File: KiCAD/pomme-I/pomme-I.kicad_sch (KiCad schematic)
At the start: 32 parts, among them J1 TV out, Q1 2N3904, SW1 SW_SPST, SW2 reset, SW3 local echo, SW4 baud rate 1, SW5 baud rate 0, T1 step down transformer, U1 LD1117V50-TO-220, U2 23LC1024, U3 25LC1024, Y1 20 Mhz

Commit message: modification schémitique
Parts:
- added D5, D6: 1N4001, Diode_THT:D_DO-41_SOD81_P10.16mm_Horizontal, symbol Diode:1N4004
- D1, D2: value 1N4004 -> 1N4001
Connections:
- net Vunreg: now reaches C1.1, D1.1 (K), D2.1 (K), U1.3 (VI)
- net Vunreg: now also D5.2 (A), D6.2 (A)
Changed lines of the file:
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@@
     (stroke (width 0) (type default) (color 0 0 0 0))
   )
+  (wire (pts (xy 106.68 124.46) (xy 106.68 114.3))
+    (stroke (width 0) (type default) (color 0 0 0 0))
+  )
   (polyline (pts (xy 153.035 39.37) (xy 169.545 39.37))
     (stroke (width 0) (type solid) (color 0 0 0 0))
@@
     (stroke (width 0) (type default) (color 0 0 0 0))
   )
+  (wire (pts (xy 156.845 60.96) (xy 156.845 53.34))
+    (stroke (width 0) (type default) (color 0 0 0 0))
+  )
   (wire (pts (xy 114.935 142.875) (xy 114.935 149.86))
     (stroke (width 0) (type default) (color 0 0 0 0))
@@
     (stroke (width 0) (type default) (color 0 0 0 0))
   )
+  (wire (pts (xy 106.68 114.3) (xy 102.87 114.3))
+    (stroke (width 0) (type default) (color 0 0 0 0))
+  )
   (wire (pts (xy 161.29 154.305) (xy 161.29 156.845))
     (stroke (width 0) (type default) (color 0 0 0 0))
@@
     (stroke (width 0) (type default) (color 0 0 0 0))
   )
+  (wire (pts (xy 154.305 53.34) (xy 156.845 53.34))
+    (stroke (width 0) (type default) (color 0 0 0 0))
+  )
   (wire (pts (xy 197.485 46.99) (xy 188.595 46.99))
     (stroke (width 0) (type default) (color 0 0 0 0))
@@
     (effects (font (size 1.27 1.27)) (justify left bottom))
   )
+  (global_label "Vunreg" (shape input) (at 146.685 53.34 180) (fields_autoplaced)
+    (effects (font (size 1 1)) (justify right))
+    (property "Références Inter-Feuilles" "${INTERSHEET_REFS}" (id 0) (at 139.7374 53.2775 0)
+      (effects (font (size 1 1)) (justify right) hide)
+    )
+  )
   (global_label "BR0" (shape input) (at 132.715 95.885 0) (fields_autoplaced)
     (effects (font (size 1 1)) (justify left))
@@
     )
   )
+  (global_label "Vunreg" (shape input) (at 95.25 114.3 180) (fields_autoplaced)
+    (effects (font (size 1 1)) (justify right))
+    (property "Références Inter-Feuilles" "${INTERSHEET_REFS}" (id 0) (at 88.3024 114.2375 0)
+      (effects (font (size 1 1)) (justify right) hide)
+    )
+  )
   (global_label "{slash}cs_ram" (shape input) (at 168.91 130.81 180) (fields_autoplaced)
     (effects (font (size 1 1)) (justify right))
@@
     )
   )
+  (global_label "Vunreg" (shape input) (at 93.345 26.035 90) (fields_autoplaced)
+    (effects (font (size 1 1)) (justify left))
+    (property "Références Inter-Feuilles" "${INTERSHEET_REFS}" (id 0) (at 93.4075 19.0874 90)
+      (effects (font (size 1 1)) (justify left) hide)
+    )
+  )
   (global_label "spi_mosi" (shape input) (at 144.145 143.51 270) (fields_autoplaced)
     (effects (font (size 1 1)) (justify right))
@@
   (symbol (lib_id "Diode:1N4004") (at 68.58 36.195 180) (unit 1)
     (in_bom yes) (on_board yes) (fields_autoplaced)
-    (property "Reference" "D2" (id 0) (at 68.58 29.845 0))
-    (property "Value" "1N4004" (id 1) (at 68.58 32.385 0))
+    (property "Reference" "D2" (id 0) (at 68.58 29.21 0))
+    (property "Value" "1N4001" (id 1) (at 68.58 31.75 0))
     (property "Footprint" "Diode_THT:D_DO-41_SOD81_P10.16mm_Horizontal" (id 2) (at 68.58 31.75 0)
       (effects (font (size 1.27 1.27)) hide)
@@
   (symbol (lib_id "Diode:1N4004") (at 68.58 26.035 180) (unit 1)
     (in_bom yes) (on_board yes) (fields_autoplaced)
-    (property "Reference" "D1" (id 0) (at 68.58 19.685 0))
-    (property "Value" "1N4004" (id 1) (at 68.58 22.225 0))
+    (property "Reference" "D1" (id 0) (at 68.58 19.05 0))
+    (property "Value" "1N4001" (id 1) (at 68.58 21.59 0))
     (property "Footprint" "Diode_THT:D_DO-41_SOD81_P10.16mm_Horizontal" (id 2) (at 68.58 21.59 0)
       (effects (font (size 1.27 1.27)) hide)
@@
     (pin "1")
   )
+  (symbol (lib_id "Diode:1N4004") (at 99.06 114.3 180) (unit 1)
+    (in_bom yes) (on_board yes) (fields_autoplaced)
+    (property "Reference" "D5" (id 0) (at 99.06 107.95 0))
+    (property "Value" "1N4001" (id 1) (at 99.06 110.49 0))
+    (property "Footprint" "Diode_THT:D_DO-41_SOD81_P10.16mm_Horizontal" (id 2) (at 99.06 109.855 0)
+      (effects (font (size 1.27 1.27)) hide)
+    )
+    (property "Datasheet" "http://www.vishay.com/docs/88503/1n4001.pdf" (id 3) (at 99.06 114.3 0)
+      (effects (font (size 1.27 1.27)) hide)
+    )
+    (pin "1")
+    (pin "2")
+  )
   (symbol (lib_id "Device:C") (at 175.895 95.25 0) (unit 1)
     (in_bom yes) (on_board yes)
@@
     (pin "1")
   )
+  (symbol (lib_id "Diode:1N4004") (at 150.495 53.34 180) (unit 1)
+    (in_bom yes) (on_board yes) (fields_autoplaced)
+    (property "Reference" "D6" (id 0) (at 150.495 46.99 0))
+    (property "Value" "1N4001" (id 1) (at 150.495 49.53 0))
+    (property "Footprint" "Diode_THT:D_DO-41_SOD81_P10.16mm_Horizontal" (id 2) (at 150.495 48.895 0)
+      (effects (font (size 1.27 1.27)) hide)
+    )
+    (property "Datasheet" "http://www.vishay.com/docs/88503/1n4001.pdf" (id 3) (at 150.495 53.34 0)
+      (effects (font (size 1.27 1.27)) hide)
+    )
+    (pin "1")
+    (pin "2")
+  )
   (symbol (lib_id "Device:R") (at 217.805 55.245 90) (unit 1)
     (in_bom yes) (on_board yes)
@@
     )
     (path "/5565b8b2-0c60-45d1-ba38-1421bd754b2c"
-      (reference "D1") (unit 1) (value "1N4004") (footprint "Diode_THT:D_DO-41_SOD81_P10.16mm_Horizontal")
+      (reference "D1") (unit 1) (value "1N4001") (footprint "Diode_THT:D_DO-41_SOD81_P10.16mm_Horizontal")
     )
     (path "/46478d7f-0dfd-4e23-9b76-9f0c0854b087"
-      (reference "D2") (unit 1) (value "1N4004") (footprint "Diode_THT:D_DO-41_SOD81_P10.16mm_Horizontal")
+      (reference "D2") (unit 1) (value "1N4001") (footprint "Diode_THT:D_DO-41_SOD81_P10.16mm_Horizontal")
     )
     (path "/0100e5db-1cfa-4dae-92cd-84a7cab45e90"
@@
       (reference "D4") (unit 1) (value "1N4148") (footprint "Diode_THT:D_DO-35_SOD27_P7.62mm_Horizontal")
     )
+    (path "/a08897a5-174f-4eea-9e27-770edb470417"
+      (reference "D5") (unit 1) (value "1N4001") (footprint "Diode_THT:D_DO-41_SOD81_P10.16mm_Horizontal")
+    )
+    (path "/d5ff0c1b-f735-41ab-bf38-10e73f4b9085"
+      (reference "D6") (unit 1) (value "1N4001") (footprint "Diode_THT:D_DO-41_SOD81_P10.16mm_Horizontal")
+    )
     (path "/45d6ba32-8b54-490b-9486-39905a5c4e74"

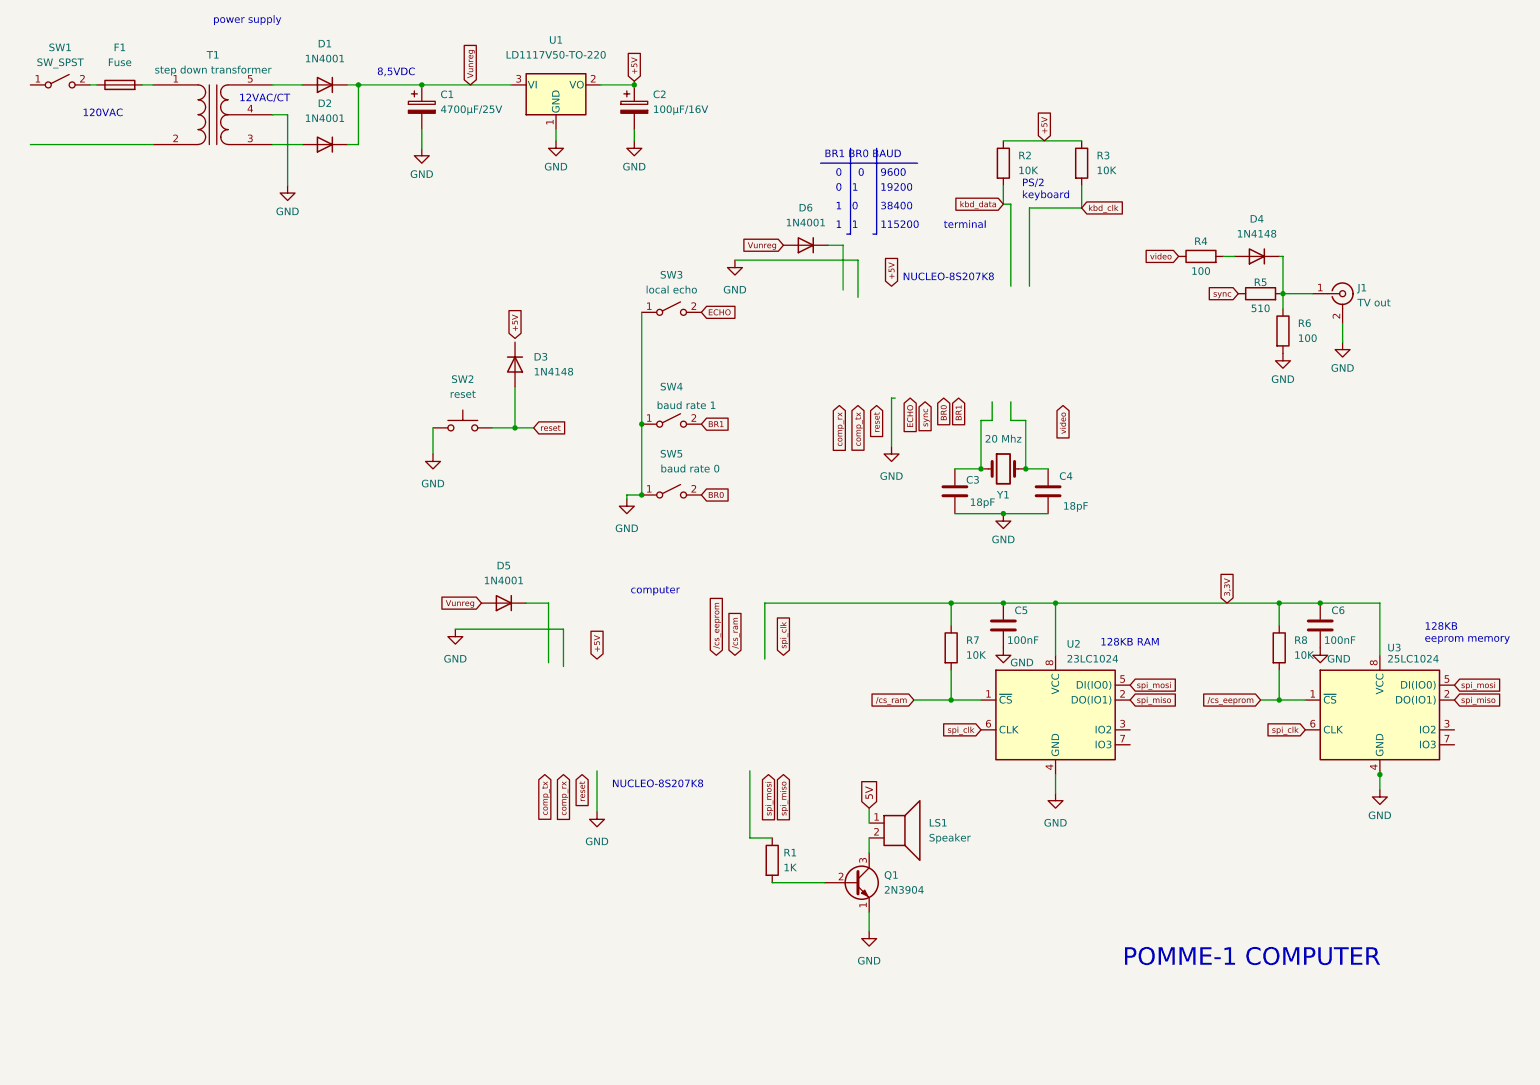
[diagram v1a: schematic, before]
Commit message: Modification à terminal.asm pour que pomme-I fonctionne avec STM8_terminal
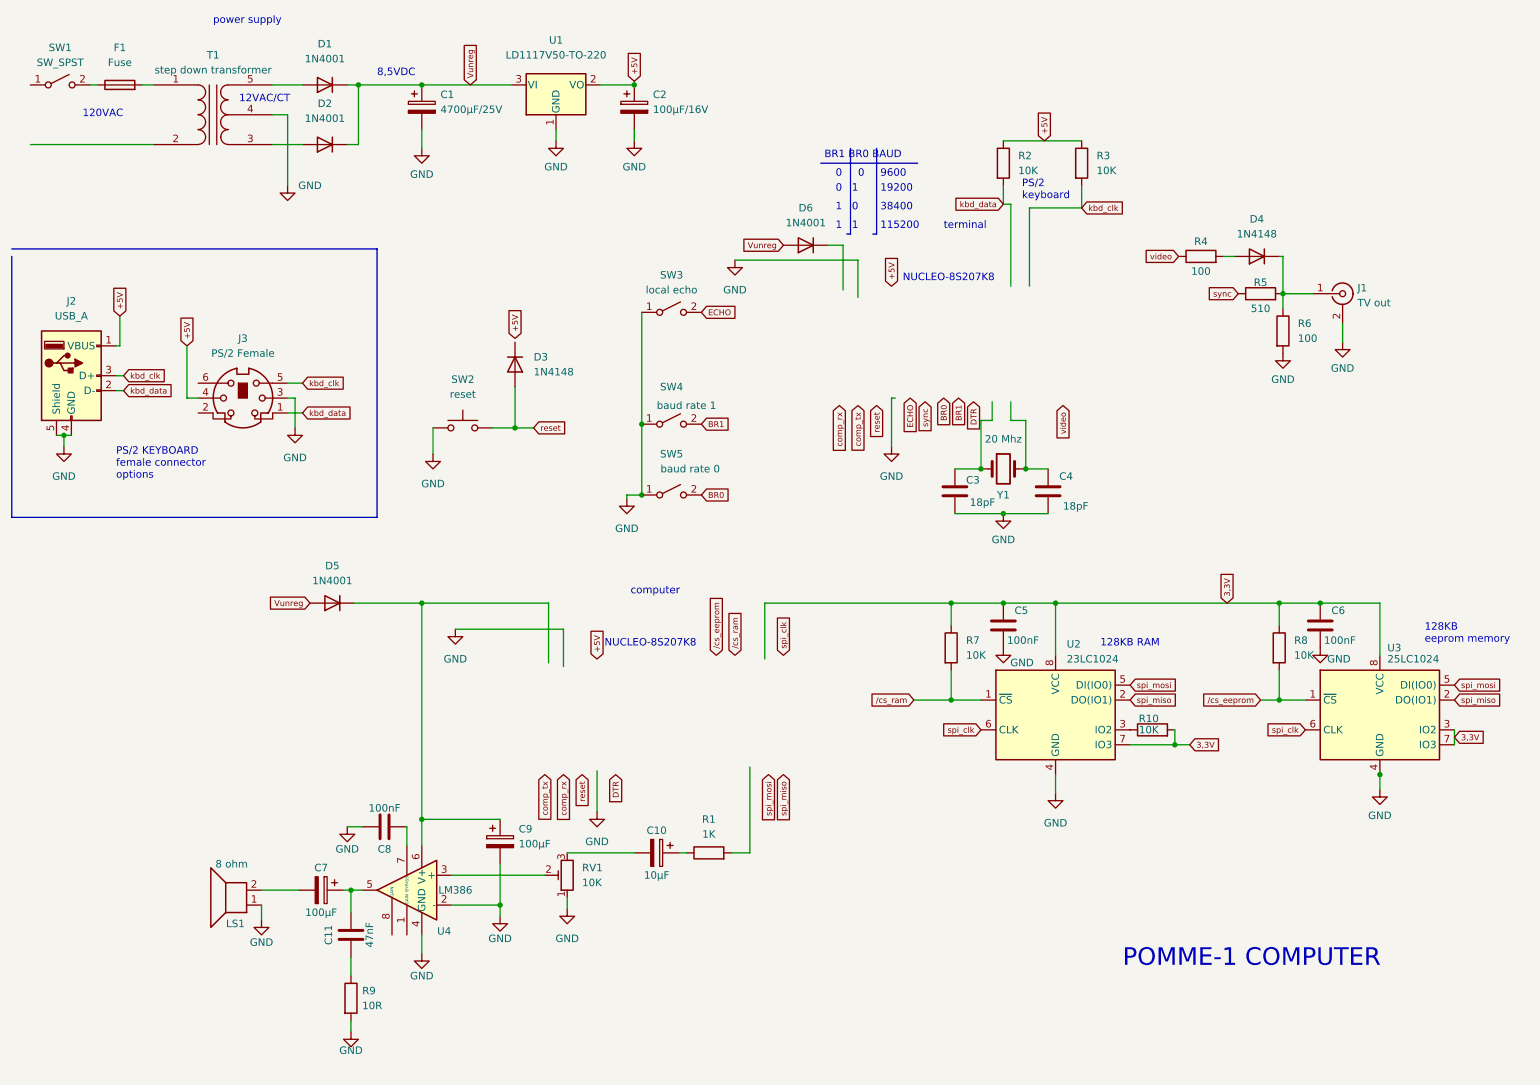
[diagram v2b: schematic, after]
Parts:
- removed Q1: 2N3904, Package_TO_SOT_THT:TO-92_Inline, symbol Transistor_BJT:2N3904
- added C10: 10µF, symbol Device:C_Polarized
- added C11: 47nF, symbol Device:C
- added C7, C9: 100µF, symbol Device:C_Polarized
- added C8: 100nF, symbol Device:C
- added J2: USB_A, symbol Connector:USB_A
- added J3: PS/2 Female, symbol Connector:Mini-DIN-6
- added R10: 10K, symbol Device:R
- added R9: 10R, symbol Device:R
- added RV1: 10K, symbol Device:R_Potentiometer_Trim
- added U4: LM386, symbol Amplifier_Audio:LM386
- LS1: value Speaker -> 8 ohm
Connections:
- net 5V is gone; now on net GND: LS1.1
- net +5V: now also J2.1 (VBUS), J3.4
- net 3,3V: now also U2.7 (IO3), U3.3 (IO2), U3.7 (IO3), R10.2
- net GND: now also C8.1, C9.2, J2.4 (GND), J2.5 (Shield), J3.3, R9.2, RV1.1, U4.2 (-), U4.4 (GND)
- net kbd_clk: now also J2.3 (D+), J3.5
- net kbd_data: now also J2.2 (D-), J3.1
- net at U2.3 (IO2): now also R10.1
- net at LS1.2: now also C7.2
- net at R1.1: now also C10.1
- net at D5.1 (K): now also C9.1, U4.6 (V+)
- new net: C8.2, U4.7 (BYPASS)
- new net: C10.2, RV1.3
- new net: RV1.2, U4.3 (+)
- new net: C11.1, C7.1, U4.5
- new net: C11.2, R9.1
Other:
- note added: "PS/2 KEYBOARD female connector options"
- moved on the sheet: D5, LS1, R1

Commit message: mise à jour schématique
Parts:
- removed SW2: reset, symbol Switch:SW_Push
- added C12, C13: 100nF, symbol Device:C
- added D7: 1N4148, Diode_THT:D_DO-35_SOD27_P7.62mm_Horizontal, symbol Diode:1N4148
- added R11, R12: 10K, symbol Device:R
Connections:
- net GND: now also C12.2, C13.2
- net 3.3V: now reaches D3.1 (K)
- net 3.3V: now also D7.1 (K), R11.1, R12.1
- net reset renamed term_reset
- net term_reset: now also C13.1, R12.2
- new net comp_reset: C12.1, D7.2 (A), R11.2

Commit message: mise à jour schématique
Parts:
- removed R10: 10K, symbol Device:R
- added C? (x2): 18pF, symbol Device:C
- added Y?: 24Mhz, symbol Device:Crystal
- renumbered C12 to C1, C3 to C10, C5 to C11, C4 to C12, C6 to C13, C7 to C2, C11 to C3, C8 to C4, C1 to C5, C9 to C6, C13 to C7, C2 to C8, C10 to C9, D7 to D1, D1 to D2, D2 to D3, D5 to D4, D3 to D5, D4 to D7, J2 to J1, J3 to J2, J1 to J3, R11 to R1, R5 to R10, R8 to R11, R6 to R12, R9 to R2, R12 to R3, R1 to R4, R7 to R5, R2 to R6, R3 to R7, R4 to R9, SW3 to SW2, SW4 to SW3, SW5 to SW4, U4 to U1, U1 to U2, U2 to U3, U3 to U4
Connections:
- net GND: now also C?.2, C?.2
- new net OSCIN: C?.1, Y?.1
- new net OSCOUT: C?.1, Y?.2
- no-connect marks 0 -> 1
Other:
- added sheet pomme-iS (pomme-IS.kicad_sch)
- note added: "optionel"
